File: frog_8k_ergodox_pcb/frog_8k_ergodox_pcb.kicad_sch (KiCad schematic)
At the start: 14 parts, among them J1 USB_C_Receptacle_USB2.0_14P, U1 PMW3360DM-T2QU, U2 STM32F072CBTx, U3 TLV74318PDBVR

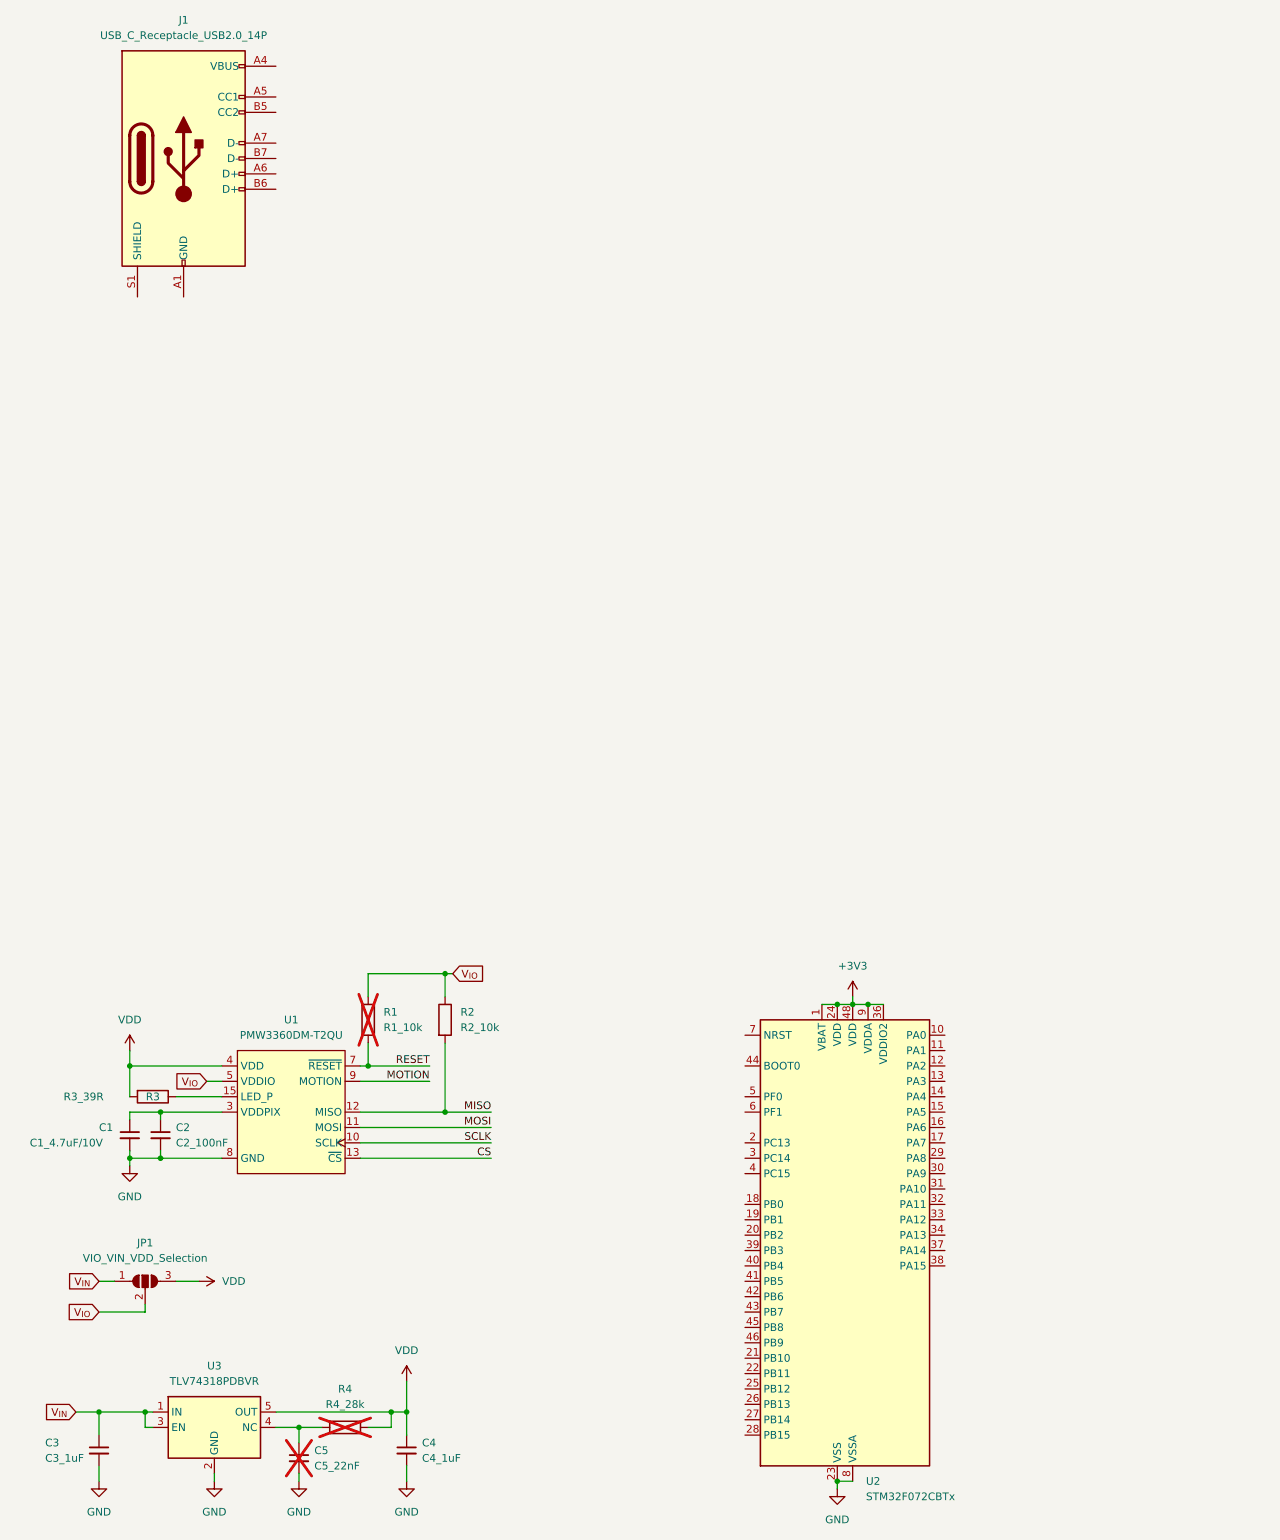
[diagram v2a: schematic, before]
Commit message: Connected pmw3360 to stm32
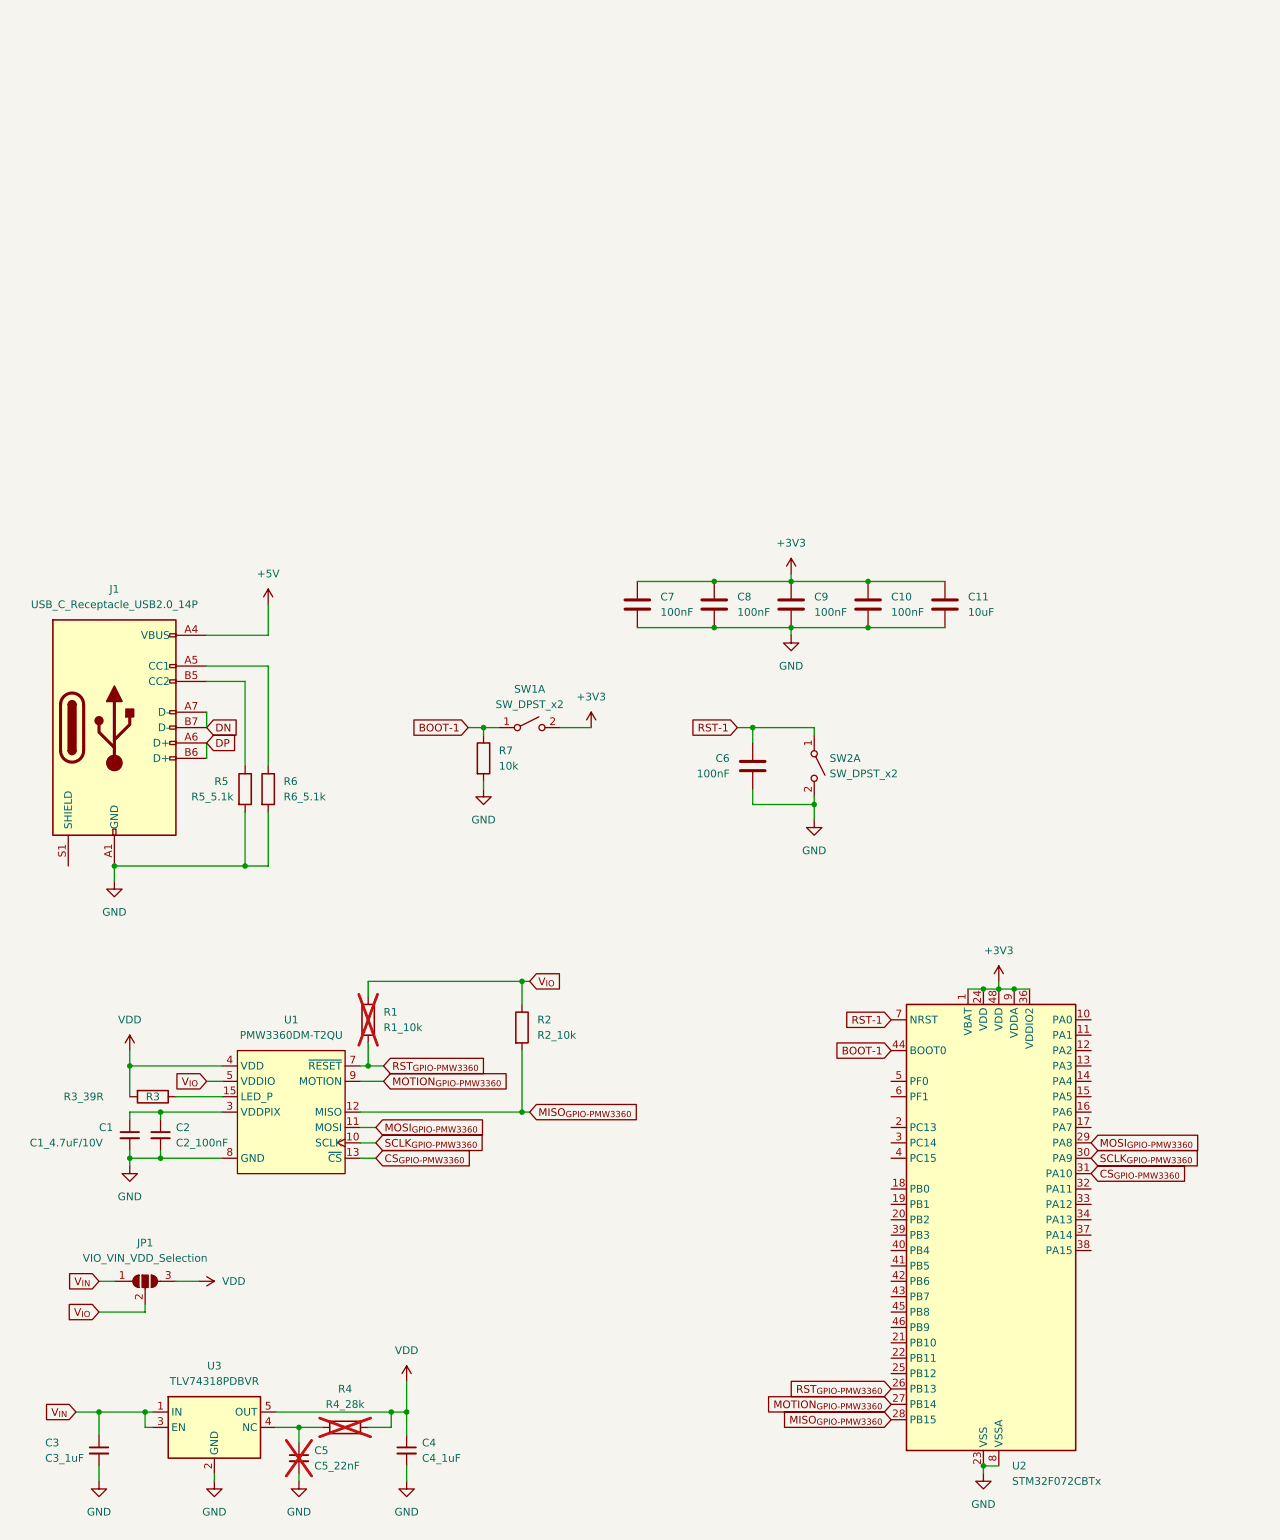
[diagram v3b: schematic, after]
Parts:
- added C10, C6, C7, C8, C9: 100nF, Capacitor_SMD:C_0402_1005Metric, symbol Device:C
- added C11: 10uF, Capacitor_SMD:C_0402_1005Metric, symbol Device:C
- added R5: R5_5.1k, Resistor_SMD:R_0805_2012Metric_Pad1.20x1.40mm_HandSolder, symbol Device:R
- added R6: R6_5.1k, Resistor_SMD:R_0805_2012Metric_Pad1.20x1.40mm_HandSolder, symbol Device:R
- added R7: 10k, Resistor_SMD:R_0402_1005Metric, symbol Device:R
- added SW1, SW2: SW_DPST_x2, Button_Switch_SMD:SW_Push_1P1T_XKB_TS-1187A, symbol Switch:SW_DPST_x2
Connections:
- net CS is gone; now on net CS_{GPIO-PMW3360}: U1.13 (~{CS})
- net MISO is gone; now on net MISO_{GPIO-PMW3360}: R2.2, U1.12 (MISO)
- net MOSI is gone; now on net MOSI_{GPIO-PMW3360}: U1.11 (MOSI)
- net MOTION is gone; now on net MOTION_{GPIO-PMW3360}: U1.9 (MOTION)
- net RESET is gone; now on net RST_{GPIO-PMW3360}: R1.2, U1.7 (~{RESET})
- net SCLK is gone; now on net SCLK_{GPIO-PMW3360}: U1.10 (SCLK)
- net +3V3: now also C10.1, C11.1, C7.1, C8.1, C9.1, SW1.2 (B)
- net GND: now also J1.A1 (GND), J1.A12 (GND), J1.B1 (GND), J1.B12 (GND), C10.2, C11.2, C6.2, C7.2, C8.2, C9.2, R5.2, R6.2, R7.2, SW2.2 (B)
- net RST_{GPIO-PMW3360}: now reaches U2.26 (PB13)
- net MOTION_{GPIO-PMW3360}: now reaches U2.27 (PB14)
- net MISO_{GPIO-PMW3360}: now reaches U2.28 (PB15)
- net MOSI_{GPIO-PMW3360}: now reaches U2.29 (PA8)
- net SCLK_{GPIO-PMW3360}: now reaches U2.30 (PA9)
- net CS_{GPIO-PMW3360}: now reaches U2.31 (PA10)
- net BOOT-1: now reaches U2.44 (BOOT0)
- net BOOT-1: now also R7.1, SW1.1 (A)
- net RST-1: now reaches U2.7 (NRST)
- net RST-1: now also C6.1, SW2.1 (A)
- net +5V: now reaches J1.A4 (VBUS), J1.A9 (VBUS), J1.B4 (VBUS), J1.B9 (VBUS)
- net at J1.A5 (CC1): now also R6.1
- net DP: now reaches J1.A6 (D+)
- net DP: now also J1.B6 (D+)
- net DN: now reaches J1.A7 (D-)
- net DN: now also J1.B7 (D-)
- net at J1.B5 (CC2): now also R5.1
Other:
- moved on the sheet: J1, R2, U2

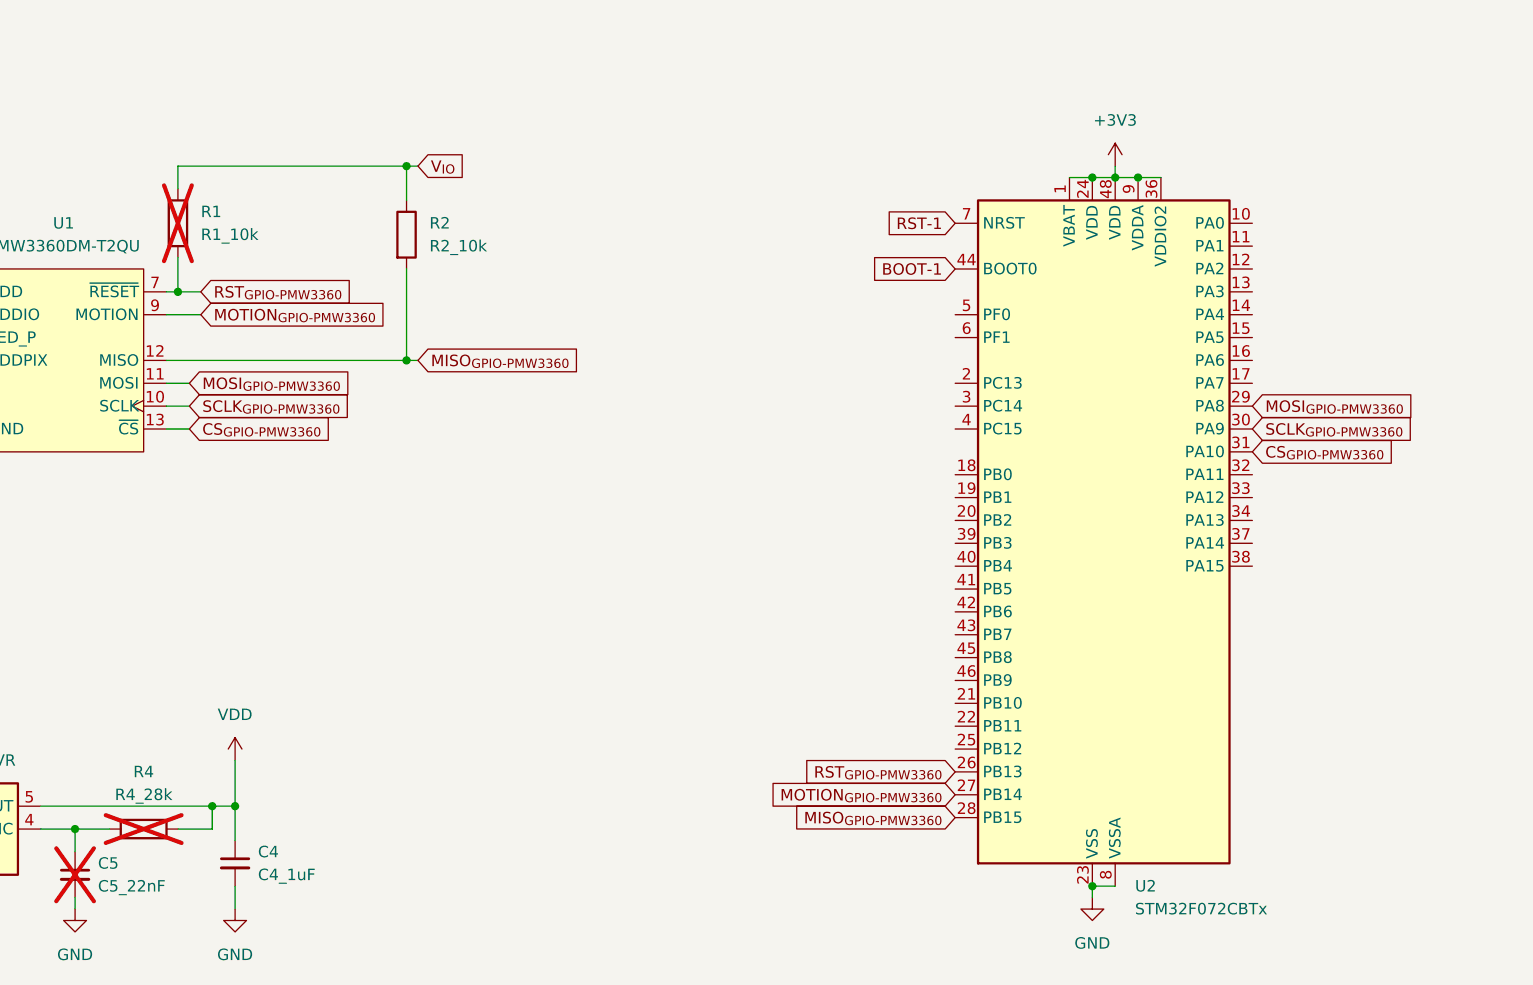
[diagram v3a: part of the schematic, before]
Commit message: Updated PMW3360's GPIO Pin.
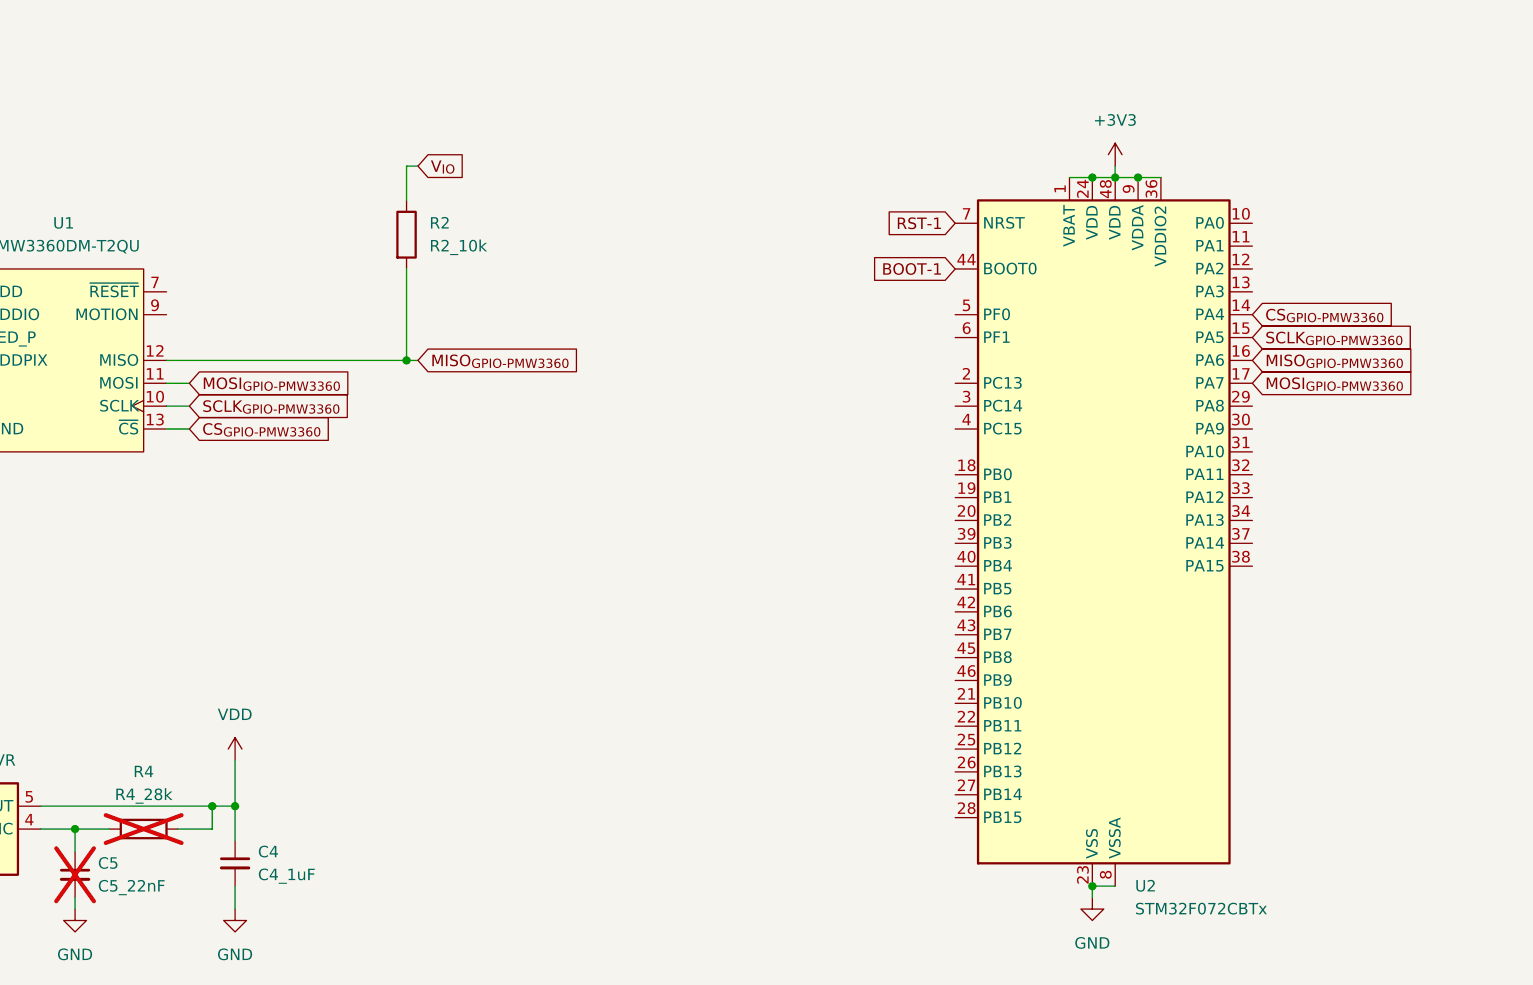
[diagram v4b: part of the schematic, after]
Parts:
- removed R1: R1_10k, Resistor_SMD:R_0805_2012Metric_Pad1.20x1.40mm_HandSolder, symbol Device:R
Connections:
- net CS_{GPIO-PMW3360}: now also U2.14 (PA4); no longer U2.31 (PA10)
- net MISO_{GPIO-PMW3360}: now also U2.16 (PA6); no longer U2.28 (PB15)
- net MOSI_{GPIO-PMW3360}: now also U2.17 (PA7); no longer U2.29 (PA8)
- net SCLK_{GPIO-PMW3360}: now also U2.15 (PA5); no longer U2.30 (PA9)
- net MOTION_{GPIO-PMW3360}: no longer names the net of U1.9 (MOTION)
- net MOTION_{GPIO-PMW3360}: no longer U2.27 (PB14)
- net RST_{GPIO-PMW3360}: no longer names the net of U1.7 (~{RESET})
- net RST_{GPIO-PMW3360}: no longer U2.26 (PB13)
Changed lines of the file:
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@@
 	)
 	(junction
-		(at 74.93 200.66)
-		(diameter 0)
-		(color 0 0 0 0)
-	)
-	(junction
 		(at 144.78 120.65)
 		(diameter 0)
@@
 	)
 	(junction
-		(at 100.33 186.69)
-		(diameter 0)
-		(color 0 0 0 0)
-	)
-	(junction
 		(at 144.78 128.27)
 		(diameter 0)
@@
 	(wire
 		(pts
-			(xy 74.93 186.69) (xy 100.33 186.69)
-		)
-		(stroke
-			(width 0)
-			(type default)
-		)
-	)
-	(wire
-		(pts
 			(xy 132.08 120.65) (xy 144.78 120.65)
 		)
@@
 	(wire
 		(pts
-			(xy 74.93 186.69) (xy 74.93 189.23)
-		)
-		(stroke
-			(width 0)
-			(type default)
-		)
-	)
-	(wire
-		(pts
 			(xy 144.78 119.38) (xy 144.78 120.65)
 		)
@@
 	(wire
 		(pts
-			(xy 73.66 203.2) (xy 77.47 203.2)
-		)
-		(stroke
-			(width 0)
-			(type default)
-		)
-	)
-	(wire
-		(pts
 			(xy 132.08 128.27) (xy 144.78 128.27)
 		)
@@
 	(wire
 		(pts
-			(xy 73.66 200.66) (xy 74.93 200.66)
-		)
-		(stroke
-			(width 0)
-			(type default)
-		)
-	)
-	(wire
-		(pts
 			(xy 49.53 269.24) (xy 49.53 267.97)
 		)
@@
 	(wire
 		(pts
-			(xy 74.93 196.85) (xy 74.93 200.66)
-		)
-		(stroke
-			(width 0)
-			(type default)
-		)
-	)
-	(wire
-		(pts
 			(xy 40.64 208.28) (xy 50.8 208.28)
 		)
@@
 	(wire
 		(pts
-			(xy 74.93 200.66) (xy 77.47 200.66)
-		)
-		(stroke
-			(width 0)
-			(type default)
-		)
-	)
-	(wire
-		(pts
 			(xy 181.61 187.96) (xy 184.15 187.96)
 		)
@@
 		)
 	)
-	(global_label "MOTION_{GPIO-PMW3360}"
-		(shape input)
-		(at 161.29 256.54 180)
-		(fields_autoplaced yes)
-		(effects
-			(font
-				(size 1.27 1.27)
-			)
-			(justify right)
-		)
-		(property "Intersheetrefs" "${INTERSHEET_REFS}"
-			(at 139.192 256.54 0)
-			(effects
-				(font
-					(size 1.27 1.27)
-				)
-				(justify right)
-				(hide yes)
-			)
-		)
-	)
 	(global_label "V_{IO}"
 		(shape input)
@@
 	(global_label "CS_{GPIO-PMW3360}"
 		(shape input)
-		(at 194.31 218.44 0)
+		(at 194.31 203.2 0)
 		(fields_autoplaced yes)
 		(effects
@@
 		)
 		(property "Intersheetrefs" "${INTERSHEET_REFS}"
-			(at 211.8722 218.44 0)
+			(at 211.8722 203.2 0)
 			(effects
 				(font
@@
 		)
 	)
-	(global_label "MOTION_{GPIO-PMW3360}"
-		(shape input)
-		(at 77.47 203.2 0)
-		(fields_autoplaced yes)
-		(effects
-			(font
-				(size 1.27 1.27)
-			)
-			(justify left)
-		)
-		(property "Intersheetrefs" "${INTERSHEET_REFS}"
-			(at 99.568 203.2 0)
-			(effects
-				(font
-					(size 1.27 1.27)
-				)
-				(justify left)
-				(hide yes)
-			)
-		)
-	)
 	(global_label "DP"
 		(shape input)
@@
 	(global_label "MOSI_{GPIO-PMW3360}"
 		(shape input)
-		(at 194.31 213.36 0)
+		(at 194.31 210.82 0)
 		(fields_autoplaced yes)
 		(effects
@@
 		)
 		(property "Intersheetrefs" "${INTERSHEET_REFS}"
-			(at 213.9889 213.36 0)
-			(effects
-				(font
-					(size 1.27 1.27)
-				)
-				(justify left)
-				(hide yes)
-			)
-		)
-	)
-	(global_label "RST_{GPIO-PMW3360}"
-		(shape input)
-		(at 77.47 200.66 0)
-		(fields_autoplaced yes)
-		(effects
-			(font
-				(size 1.27 1.27)
-			)
-			(justify left)
-		)
-		(property "Intersheetrefs" "${INTERSHEET_REFS}"
-			(at 95.9998 200.66 0)
+			(at 213.9889 210.82 0)
 			(effects
 				(font
@@
 		)
 	)
-	(global_label "RST_{GPIO-PMW3360}"
-		(shape input)
-		(at 161.29 254 180)
-		(fields_autoplaced yes)
-		(effects
-			(font
-				(size 1.27 1.27)
-			)
-			(justify right)
-		)
-		(property "Intersheetrefs" "${INTERSHEET_REFS}"
-			(at 142.7602 254 0)
-			(effects
-				(font
-					(size 1.27 1.27)
-				)
-				(justify right)
-				(hide yes)
-			)
-		)
-	)
 	(global_label "MISO_{GPIO-PMW3360}"
 		(shape input)
-		(at 161.29 259.08 180)
+		(at 194.31 208.28 0)
 		(fields_autoplaced yes)
 		(effects
@@
 				(size 1.27 1.27)
 			)
-			(justify right)
+			(justify left)
 		)
 		(property "Intersheetrefs" "${INTERSHEET_REFS}"
-			(at 141.6111 259.08 0)
+			(at 213.9889 208.28 0)
 			(effects
 				(font
 					(size 1.27 1.27)
 				)
-				(justify right)
+				(justify left)
 				(hide yes)
 			)
@@
 	(global_label "SCLK_{GPIO-PMW3360}"
 		(shape input)
-		(at 194.31 215.9 0)
+		(at 194.31 205.74 0)
 		(fields_autoplaced yes)
 		(effects
@@
 		)
 		(property "Intersheetrefs" "${INTERSHEET_REFS}"
-			(at 214.1703 215.9 0)
+			(at 214.1703 205.74 0)
 			(effects
 				(font
@@
 					(unit 1)
 				)
-			)
-		)
-	)
-	(symbol
-		(lib_id "Device:R")
-		(at 74.93 193.04 0)
-		(unit 1)
-		(exclude_from_sim no)
-		(in_bom yes)
-		(on_board yes)
-		(dnp yes)
-		(fields_autoplaced yes)
-		(property "Reference" "R1"
-			(at 77.47 191.7699 0)
-			(effects
-				(font
-					(size 1.27 1.27)
-				)
-				(justify left)
-			)
-		)
-		(property "Value" "R1_10k"
-			(at 77.47 194.3099 0)
-			(effects
-				(font
-					(size 1.27 1.27)
-				)
-				(justify left)
-			)
-		)
-		(property "Footprint" "Resistor_SMD:R_0805_2012Metric_Pad1.20x1.40mm_HandSolder"
-			(at 73.152 193.04 90)
-			(effects
-				(font
-					(size 1.27 1.27)
-				)
-				(hide yes)
-			)
-		)
-		(property "Datasheet" "~"
-			(at 74.93 193.04 0)
-			(effects
-				(font
-					(size 1.27 1.27)
-				)
-				(hide yes)
-			)
-		)
-		(property "Description" "Resistor"
-			(at 74.93 193.04 0)
-			(effects
-				(font
-					(size 1.27 1.27)
-				)
-				(hide yes)
-			)
-		)
-		(pin "2"
-		)
-		(pin "1"
-		)
-		(instances
-			(project ""
-				(path "/34ddd234-11af-4a66-9186-ea72bce9a0a9"
-					(reference "R1")
-					(unit 1)
-				)
